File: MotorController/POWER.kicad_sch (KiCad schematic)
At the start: 0 parts

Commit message: Lots of Updates
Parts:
- added C?: 0.01uF, symbol Device:C_Small
- added C? (x2): 1uF, symbol Device:C_Small
- added C? (x2): 10uF, symbol Device:C_Small
- added D?: D_Small_Filled, symbol Device:D_Small_Filled
- added D? (x2): D_Schottky_Small_Filled, symbol Device:D_Schottky_Small_Filled
- added L?: 2.889uH, symbol Device:L_Small
- added R?: 572k, symbol Device:R_Small_US
- added R?: 100k, symbol Device:R_Small_US
- added R? (x2): 10k, symbol Device:R_Small_US
- added R?: 16.4k, symbol Device:R_Small_US
- added R?: 52.5k, symbol Device:R_Small_US
- added U?: LP38692MP-ADJ, symbol ProjectSymbols:LP38692MP-ADJ
- added U?: LMR12010YMKE, symbol ProjectSymbols:LMR12010YMKE
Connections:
- new net: C?.1, D?.1 (K), U?.1 (BOOST)
- new net: C?.2, D?.1 (K), L?.1, U?.6 (SW)
- new net: R?.1, R?.2, U?.2 (ADJ)
- new net: R?.1, R?.2, U?.3 (FB)
- new net +3V3: C?.1, R?.1, U?.3 (OUT)
- new net +5V: C?.1, C?.1, D?.1 (K), L?.2, R?.1, U?.1 (EN), U?.4 (IN)
- new net +BATT: C?.1, D?.2 (A), R?.1, U?.4 (EN), U?.5 (VIN)
- new net +VBAT_VSENSE: R?.1, R?.2
- new net +VUSB: D?.2 (A)
- new net GND: C?.2, C?.2, C?.2, C?.2, D?.2 (A), R?.2, R?.2, R?.2, U?.2 (GND), U?.5 (GND)
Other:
- note added: "3 MHz @ 11.1Vin - ~2.54uH 3 Mhz @ 16.8Vin - ~3.24uH Average of Min/Max - ~2.889uH"

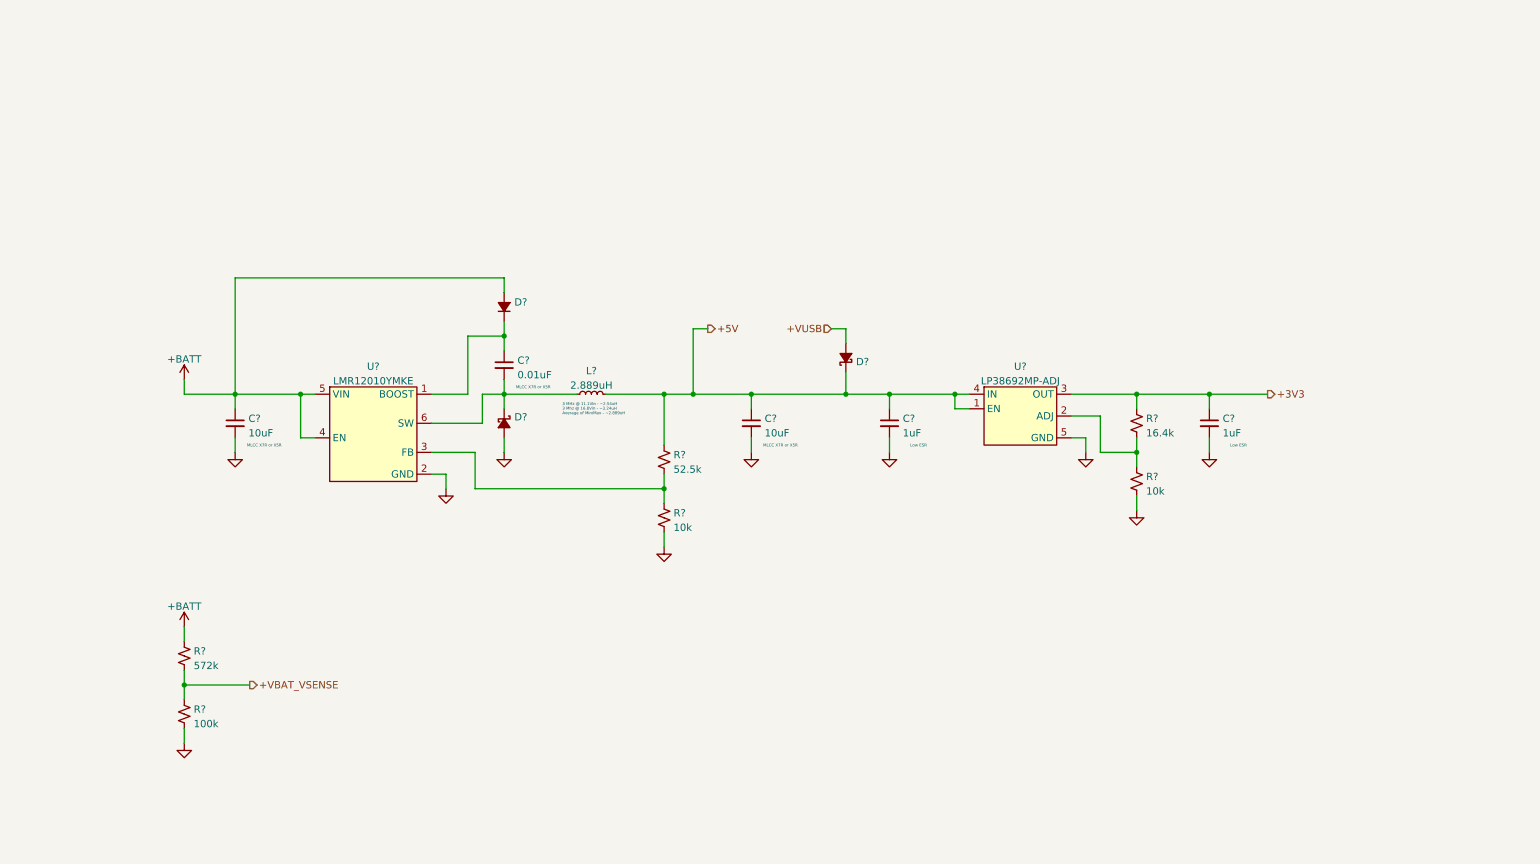
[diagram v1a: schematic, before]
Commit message: Schematic Updates
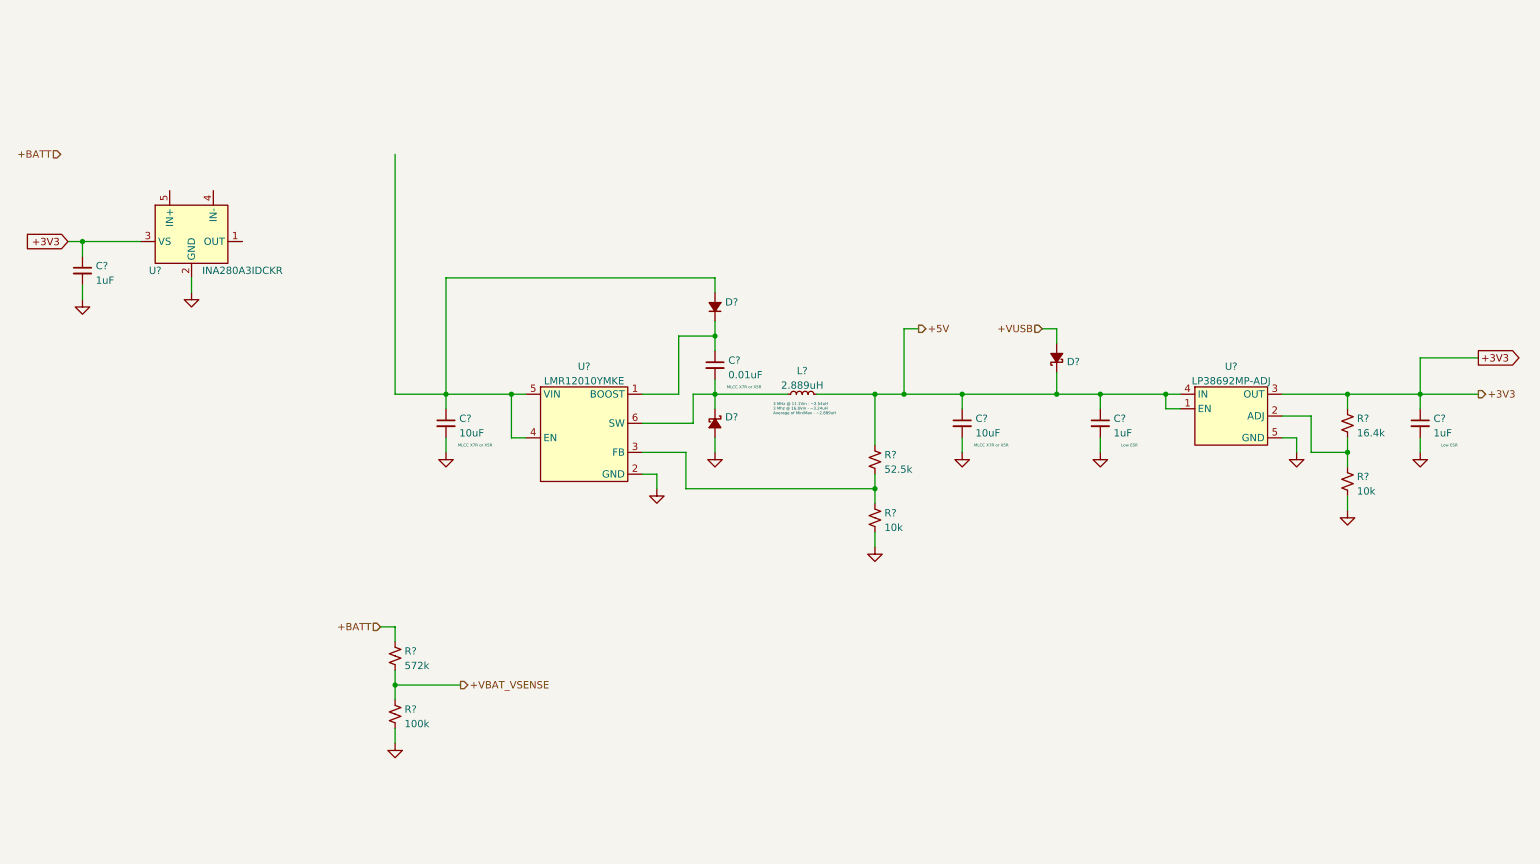
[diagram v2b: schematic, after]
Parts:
- added C?: 1uF, symbol Device:C_Small
- added U?: INA280A3IDCKR, symbol ProjectSymbols:INA280A3IDCKR
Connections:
- net +3V3: now also C?.1, U?.3 (VS)
- net +BATT: no longer C?.1, D?.2 (A), U?.4 (EN), U?.5 (VIN)
- net GND: now also C?.2, U?.2 (GND)
- new net: C?.1, D?.2 (A), U?.4 (EN), U?.5 (VIN)
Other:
- moved on the sheet: C?, D?, L?, R?, U?

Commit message: Updates
Updates
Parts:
- removed C?: 1uF, symbol Device:C_Small
- removed U?: INA280A3IDCKR, symbol ProjectSymbols:INA280A3IDCKR
- added C? (x2): 1uF, symbol Device:C_Small
- added R? (x2): 0.2mOhms, symbol Device:R_Small_US
- added U? (x2): INA280A3IDCKR, symbol ProjectSymbols:INA280A3IDCKR
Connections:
- net +3V3: now also C?.1, C?.1, U?.3 (VS), U?.3 (VS)
- net GND: now also C?.2, C?.2, U?.2 (GND), U?.2 (GND)

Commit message: More updates
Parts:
- removed C?: 1uF, symbol Device:C_Small
- removed R?: 0.2mOhms, symbol Device:R_Small_US
- removed U?: INA280A3IDCKR, symbol ProjectSymbols:INA280A3IDCKR
- added C? (x2): DNU, symbol Device:C_Small
- added C?: 1uF, symbol Device:C_Small
- added R? (x4): 0, symbol Device:R_Small_US
- added R?: 0.2mOhms, symbol Device:R_Small_US
- added U?: INA280A3IDCKR, symbol ProjectSymbols:INA280A3IDCKR
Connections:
- net +3V3: now also C?.1, U?.3 (VS)
- net +BATT: now also C?.1, D?.2 (A), R?.1, U?.4 (EN), U?.5 (VIN), R?.1, R?.1, R?.1
- net +MOTOR_VBAT: now also R?.2, R?.2
- net +XT_VBAT: now also R?.2, R?.2
- net GND: now also C?.2, U?.2 (GND)
- net MOTOR_ISENSE: now reaches U?.1 (OUT)
- net at U?.4 (IN-): now also C?.2, R?.1
- net at U?.5 (IN+): now also C?.1, R?.2
- new net: C?.2, R?.1, U?.4 (IN-)
- new net: C?.1, R?.2, U?.5 (IN+)
- new net XT_ISENSE: U?.1 (OUT)

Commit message: Updates
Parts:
- C1, C5: renamed from C?; footprint (none) -> Capacitor_SMD:C_0603_1608Metric; MPN (none) -> CC0603MRX5R8BB106
- C2, C6, C7, C9: renamed from C?; footprint (none) -> Capacitor_SMD:C_0603_1608Metric; MPN (none) -> CC0603KRX5R8BB105
- C3, C8: renamed from C?; footprint (none) -> Capacitor_SMD:C_0603_1608Metric
- C4: renamed from C?; footprint (none) -> Capacitor_SMD:C_0603_1608Metric; MPN (none) -> CC0603KRX7R8BB103
- D2, D3: renamed from D?; footprint (none) -> Diode_SMD:D_SOD-123F
- L1: renamed from L?; footprint (none) -> Footprints:XGL5050-282MEC; MPN (none) -> XGL5050-282MEC
- R1: renamed from R?; footprint (none) -> Resistor_SMD:R_0603_1608Metric; MPN (none) -> RC0603FR-07576KL
- R10, R3, R5, R8: renamed from R?; footprint (none) -> Resistor_SMD:R_0603_1608Metric; MPN PU5931FKHPA0U2L -> RC0603FR-070RL
- R11: renamed from R?; value 16.4k -> 16.5k; footprint (none) -> Resistor_SMD:R_0603_1608Metric; MPN (none) -> RC0603FR-0716K5L
- R12, R7: renamed from R?; footprint (none) -> Resistor_SMD:R_0603_1608Metric; MPN (none) -> RC0603FR-0710KL
- R2: renamed from R?; footprint (none) -> Resistor_SMD:R_0603_1608Metric; MPN (none) -> RC0603FR-07100KL
- R4, R9: renamed from R?; footprint (none) -> Footprints:RES_WSK12161L000FEA; MPN PU5931FKHPA0U2L -> WSK1216L2000FEA
- R6: renamed from R?; value 52.5k -> 52.3k; footprint (none) -> Resistor_SMD:R_0603_1608Metric; MPN (none) -> RC0603FR-0752K3L
- U1: renamed from U?; footprint (none) -> Package_TO_SOT_SMD:TSOT-23-6; MPN (none) -> LMR12010YMKE
- U2, U3: renamed from U?; footprint (none) -> Package_TO_SOT_SMD:SOT-353_SC-70-5; MPN (none) -> INA280A3IDCKR
- U4: renamed from U?; footprint (none) -> Package_TO_SOT_SMD:SOT-223-5; MPN (none) -> LP38692MP-ADJ
- gave numbers to parts that had none: 1

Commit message: Changes
Changes
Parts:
- added D? (x2): GREEN, LED_SMD:LED_0603_1608Metric, symbol Device:LED_Small
- added R? (x2): 680, Resistor_SMD:R_0402_1005Metric, symbol Device:R_Small_US
- D1: footprint (none) -> Diode_SMD:D_SMA
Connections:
- net +3V3: now also R?.2
- net +5V: now also R?.2
- net GND: now also D?.1 (K), D?.1 (K)
- new net: D?.2 (A), R?.1 (x2)
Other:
- moved on the sheet: C5, C9

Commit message: So many updates
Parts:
- added C26: 1uF, Capacitor_SMD:C_0402_1005Metric, symbol Device:C_Small
- added C27: DNU, Capacitor_SMD:C_0402_1005Metric, symbol Device:C_Small
- added R36, R38: 0, Resistor_SMD:R_0402_1005Metric, symbol Device:R_Small_US
- added R37: 0.2mOhms, Footprints:RES_WSK12161L000FEA, symbol Device:R_Small_US
- added U14: INA280A3IDCKR, Package_TO_SOT_SMD:SOT-353_SC-70-5, symbol ProjectSymbols:INA280A3IDCKR
- C2, C6, C7, C9: footprint Capacitor_SMD:C_0603_1608Metric -> Capacitor_SMD:C_0402_1005Metric; MPN CC0603KRX5R8BB105 -> CC0402KRX5R8BB105
- C3, C8: footprint Capacitor_SMD:C_0603_1608Metric -> Capacitor_SMD:C_0402_1005Metric
- C4: footprint Capacitor_SMD:C_0603_1608Metric -> Capacitor_SMD:C_0402_1005Metric; MPN CC0603KRX7R8BB103 -> CC0402KRX7R8BB103
- R1: footprint Resistor_SMD:R_0603_1608Metric -> Resistor_SMD:R_0402_1005Metric; MPN RC0603FR-07576KL -> RC0402FR-07576KL
- R10, R3, R5, R8: footprint Resistor_SMD:R_0603_1608Metric -> Resistor_SMD:R_0402_1005Metric; MPN RC0603FR-070RL -> RC0402JR-070RL
- R11: footprint Resistor_SMD:R_0603_1608Metric -> Resistor_SMD:R_0402_1005Metric; MPN RC0603FR-0716K5L -> RC0402FR-0716K5L
- R12, R7: footprint Resistor_SMD:R_0603_1608Metric -> Resistor_SMD:R_0402_1005Metric; MPN RC0603FR-0710KL -> RC0402JR-0710KL
- R2: footprint Resistor_SMD:R_0603_1608Metric -> Resistor_SMD:R_0402_1005Metric; MPN RC0603FR-07100KL -> RC0402JR-07100KL
- R6: footprint Resistor_SMD:R_0603_1608Metric -> Resistor_SMD:R_0402_1005Metric; MPN RC0603FR-0752K3L -> RC0402FR-0752K3L
- gave numbers to parts that had none: 4
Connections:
- net +3V3: now also C26.1, U14.3 (VS)
- net +BATT: now also R36.1, R37.1
- net GND: now also C26.2, U14.2 (GND)
- net +MOTOR_VBAT renamed +LMOTOR_VBAT
- net MOTOR_ISENSE renamed LMOTOR_ISENSE
- new net: C27.2, R38.1, U14.4 (IN-)
- new net: C27.1, R36.2, U14.5 (IN+)
- new net +RMOTOR_VBAT: R37.2, R38.2
- new net RMOTOR_ISENSE: U14.1 (OUT)

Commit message: my god
my god
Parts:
- removed U4: LP38692MP-ADJ, Package_TO_SOT_SMD:SOT-223-5, symbol ProjectSymbols:LP38692MP-ADJ
- added U4: AP7366-W5-7, Footprints:AP7366-W5-7, symbol ProjectSymbols:AP7366-W5-7
- R11: value 16.5k -> 52.3k; MPN RC0402FR-0716K5L -> RC0402FR-0752K3L
- R12: value 10k -> 16.5k; MPN RC0402JR-0710KL -> RC0402FR-0716K5L
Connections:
- net +3V3: now also U4.5 (OUT)
- net +5V: now also U4.1 (IN), U4.3 (EN)
- net GND: now also U4.2 (GND)
- net at R11.2, R12.1: now also U4.4 (ADJ)
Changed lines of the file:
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@@
   (junction (at 113.03 33.02) (diameter 0) (color 0 0 0 0)
   )
+  (junction (at 133.35 83.82) (diameter 0) (color 0 0 0 0)
+  )
+  (junction (at 256.54 83.82) (diameter 0) (color 0 0 0 0)
+  )
+  (junction (at 110.49 22.86) (diameter 0) (color 0 0 0 0)
+  )
+  (junction (at 170.18 83.82) (diameter 0) (color 0 0 0 0)
+  )
+  (junction (at 243.84 83.82) (diameter 0) (color 0 0 0 0)
+  )
+  (junction (at 212.09 33.02) (diameter 0) (color 0 0 0 0)
+  )
+  (junction (at 97.79 83.82) (diameter 0) (color 0 0 0 0)
+  )
+  (junction (at 219.71 33.02) (diameter 0) (color 0 0 0 0)
+  )
+  (junction (at 166.37 83.82) (diameter 0) (color 0 0 0 0)
+  )
+  (junction (at 151.13 151.13) (diameter 0) (color 0 0 0 0)
+  )
+  (junction (at 243.84 93.98) (diameter 0) (color 0 0 0 0)
+  )
   (junction (at 212.09 83.82) (diameter 0) (color 0 0 0 0)
   )
-  (junction (at 133.35 83.82) (diameter 0) (color 0 0 0 0)
-  )
-  (junction (at 256.54 83.82) (diameter 0) (color 0 0 0 0)
-  )
-  (junction (at 110.49 22.86) (diameter 0) (color 0 0 0 0)
-  )
-  (junction (at 170.18 83.82) (diameter 0) (color 0 0 0 0)
-  )
-  (junction (at 243.84 83.82) (diameter 0) (color 0 0 0 0)
-  )
-  (junction (at 212.09 33.02) (diameter 0) (color 0 0 0 0)
-  )
-  (junction (at 97.79 83.82) (diameter 0) (color 0 0 0 0)
-  )
-  (junction (at 219.71 33.02) (diameter 0) (color 0 0 0 0)
-  )
-  (junction (at 166.37 83.82) (diameter 0) (color 0 0 0 0)
-  )
-  (junction (at 151.13 151.13) (diameter 0) (color 0 0 0 0)
-  )
-  (junction (at 243.84 93.98) (diameter 0) (color 0 0 0 0)
-  )
   (junction (at 166.37 139.7) (diameter 0) (color 0 0 0 0)
   )
@@
     (stroke (width 0) (type default) (color 0 0 0 0))
   )
-  (wire (pts (xy 212.09 83.82) (xy 212.09 86.36))
-    (stroke (width 0) (type default) (color 0 0 0 0))
-  )
   (wire (pts (xy 254 96.52) (xy 254 101.6))
     (stroke (width 0) (type default) (color 0 0 0 0))
@@
     (stroke (width 0) (type default) (color 0 0 0 0))
   )
+  (wire (pts (xy 212.09 83.82) (xy 212.09 87.63))
+    (stroke (width 0) (type default) (color 0 0 0 0))
+  )
   (wire (pts (xy 262.89 83.82) (xy 262.89 86.36))
     (stroke (width 0) (type default) (color 0 0 0 0))
@@
     (stroke (width 0) (type default) (color 0 0 0 0))
   )
-  (wire (pts (xy 212.09 83.82) (xy 214.63 83.82))
-    (stroke (width 0) (type default) (color 0 0 0 0))
-  )
   (wire (pts (xy 151.13 151.13) (xy 161.29 151.13))
     (stroke (width 0) (type default) (color 0 0 0 0))
@@
     (stroke (width 0) (type default) (color 0 0 0 0))
   )
+  (wire (pts (xy 212.09 83.82) (xy 215.9 83.82))
+    (stroke (width 0) (type default) (color 0 0 0 0))
+  )
   (wire (pts (xy 232.41 91.44) (xy 234.95 91.44))
     (stroke (width 0) (type default) (color 0 0 0 0))
@@
     (stroke (width 0) (type default) (color 0 0 0 0))
   )
-  (wire (pts (xy 214.63 86.36) (xy 212.09 86.36))
+  (wire (pts (xy 212.09 87.63) (xy 215.9 87.63))
     (stroke (width 0) (type default) (color 0 0 0 0))
   )
@@
     (pin "1")
     (pin "2")
-  )
-  (symbol (lib_id "ProjectSymbols:LP38692MP-ADJ") (at 223.52 87.63 0) (unit 1)
-    (in_bom yes) (on_board yes) (fields_autoplaced)
-    (property "Reference" "U4" (id 0) (at 223.52 78.9772 0))
-    (property "Value" "LP38692MP-ADJ" (id 1) (at 223.52 81.5141 0))
-    (property "Footprint" "Package_TO_SOT_SMD:SOT-223-5" (id 2) (at 223.52 76.2 0)
-      (effects (font (size 1.27 1.27)) hide)
-    )
-    (property "Datasheet" "" (id 3) (at 223.52 76.2 0)
-      (effects (font (size 1.27 1.27)) hide)
-    )
-    (property "MPN" "LP38692MP-ADJ" (id 4) (at 223.52 87.63 0)
-      (effects (font (size 1.27 1.27)) hide)
-    )
-    (pin "1")
-    (pin "2")
-    (pin "3")
-    (pin "4")
-    (pin "5")
   )
   (symbol (lib_id "Device:C_Small") (at 86.36 88.9 0) (unit 1)
@@
       (effects (font (size 1.27 1.27)) (justify left))
     )
-    (property "Value" "10k" (id 1) (at 245.491 100.7622 0)
+    (property "Value" "16.5k" (id 1) (at 245.491 100.7622 0)
       (effects (font (size 1.27 1.27)) (justify left))
     )
@@
       (effects (font (size 1.27 1.27)) hide)
     )
-    (property "MPN" "RC0402JR-0710KL" (id 4) (at 243.84 99.06 0)
+    (property "MPN" "RC0402FR-0716K5L" (id 4) (at 243.84 99.06 0)
       (effects (font (size 1.27 1.27)) hide)
     )
@@
       (effects (font (size 1.27 1.27)) (justify left))
     )
-    (property "Value" "16.5k" (id 1) (at 245.491 90.6022 0)
+    (property "Value" "52.3k" (id 1) (at 245.491 90.6022 0)
       (effects (font (size 1.27 1.27)) (justify left))
     )
@@
       (effects (font (size 1.27 1.27)) hide)
     )
-    (property "MPN" "RC0402FR-0716K5L" (id 4) (at 243.84 88.9 0)
+    (property "MPN" "RC0402FR-0752K3L" (id 4) (at 243.84 88.9 0)
       (effects (font (size 1.27 1.27)) hide)
     )
@@
     (pin "1")
   )
+  (symbol (lib_id "ProjectSymbols:AP7366-W5-7") (at 222.25 86.36 0) (unit 1)
+    (in_bom yes) (on_board yes) (fields_autoplaced)
+    (property "Reference" "U4" (id 0) (at 224.155 77.47 0))
+    (property "Value" "AP7366-W5-7" (id 1) (at 224.155 80.01 0))
+    (property "Footprint" "Footprints:AP7366-W5-7" (id 2) (at 222.25 72.39 0)
+      (effects (font (size 1.27 1.27)) hide)
+    )
+    (property "Datasheet" "" (id 3) (at 222.25 72.39 0)
+      (effects (font (size 1.27 1.27)) hide)
+    )
+    (property "MPN" "AP7366-W5-7" (id 4) (at 222.25 86.36 0)
+      (effects (font (size 1.27 1.27)) hide)
+    )
+    (pin "1")
+    (pin "2")
+    (pin "3")
+    (pin "4")
+    (pin "5")
+  )
   (symbol (lib_id "power:GND") (at 86.36 93.98 0) (unit 1)
